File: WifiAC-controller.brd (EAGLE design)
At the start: 55.9 x 53.3 mm, 10 parts

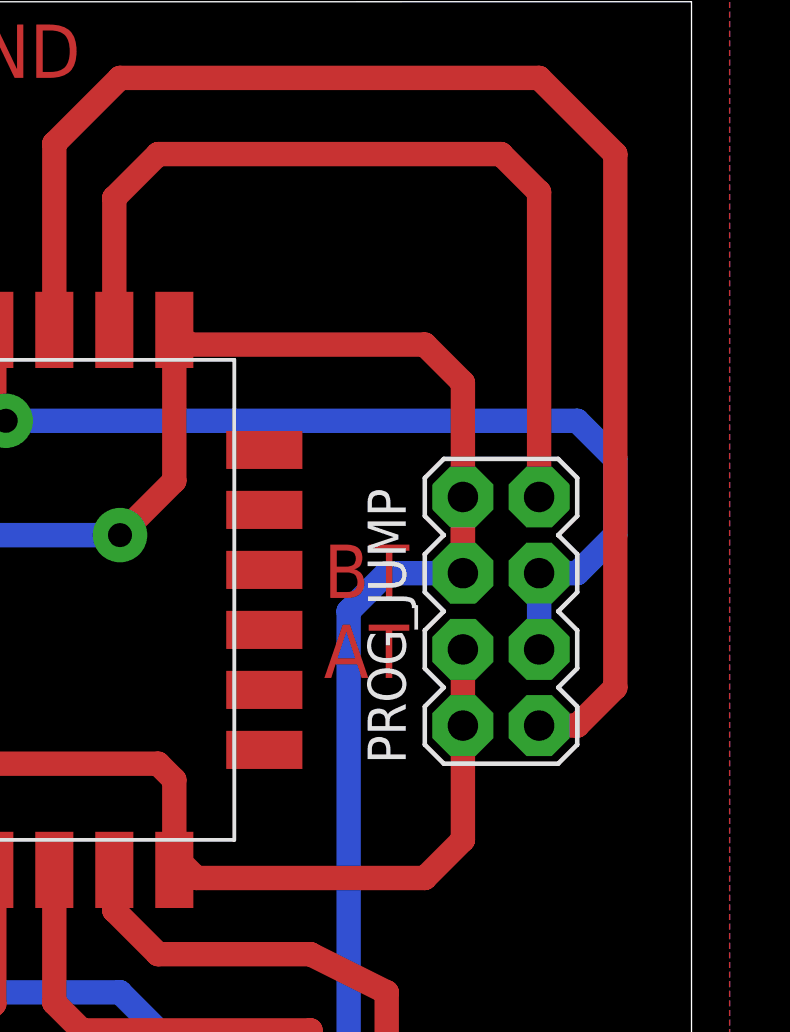
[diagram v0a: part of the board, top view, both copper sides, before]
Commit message: updated schematic to add input connections for the esp module
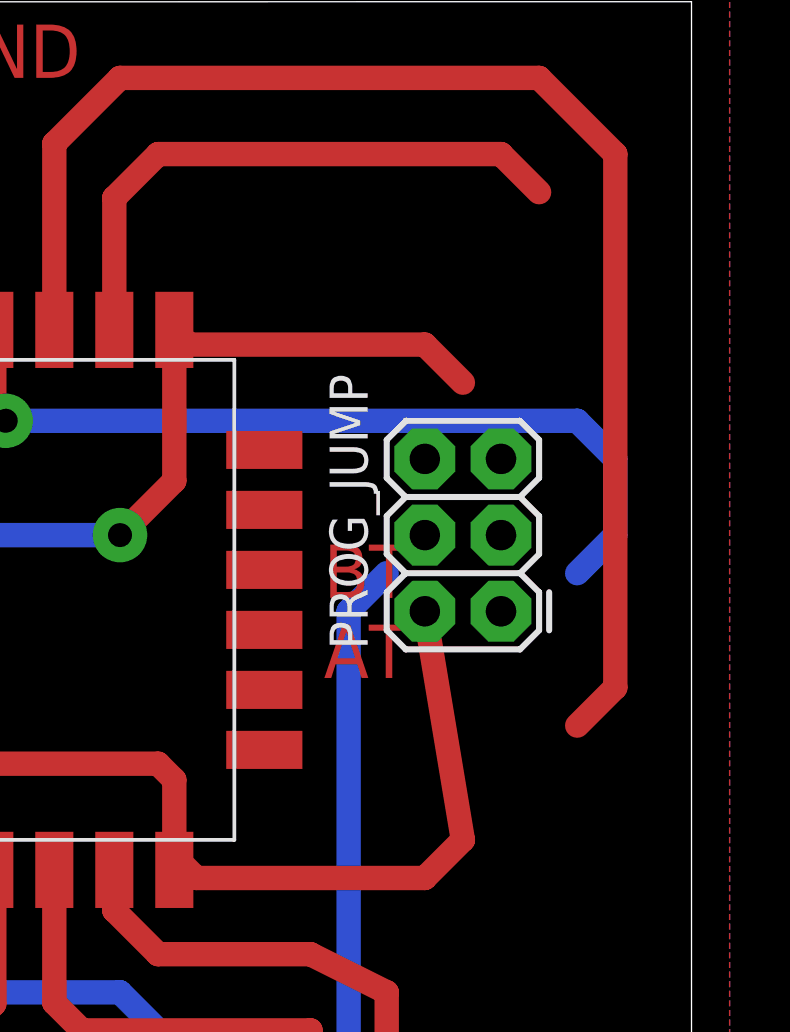
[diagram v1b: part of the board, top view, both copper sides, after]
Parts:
- PROG_JUMP: value (none) -> FEMALE 2x3; device SparkFun-Connectors:2X4 -> SparkFun-Connectors:2X3
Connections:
- net 3V3: no longer PROG_JUMP.4
- net GND: now also PROG_JUMP.4; no longer PROG_JUMP.8
- net GPIO0: no longer PROG_JUMP.5
- net GPIO15: now also PROG_JUMP.5; no longer PROG_JUMP.7
- net P5: now also ESP-12E.GPIO9
- net P58: now also ESP-12E.CSO
- net P59: now also ESP-12E.MISO
- net P6: now also ESP-12E.GPIO10
- net P7: now also ESP-12E.MOSI
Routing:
- net GND: track 123.9 -> 112.5 mm
- net GPIO15: track 29.9 -> 19.7 mm
- net GPIO0: track 32.2 -> 28.4 mm
- net 3V3: track 69.6 -> 71.0 mm
- net GPIO2: track 47.7 -> 46.4 mm
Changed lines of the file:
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@@
 </element>
 <element name="ESP-12E" library="ESP-12E" package="ESP-07/12" value="ESP-07/12_ESP-12E" x="40.64" y="25.4" rot="R90"/>
-<element name="PROG_JUMP" library="SparkFun-Connectors" package="2X4" value="" x="49.53" y="33.02" rot="R90"/>
+<element name="PROG_JUMP" library="SparkFun-Connectors" package="2X3" value="FEMALE 2x3" x="49.53" y="33.02" rot="R90">
+<attribute name="VALUE" value="FEMALE 2x3" x="49.53" y="33.02" size="1.778" layer="27" rot="R90" display="off"/>
+<attribute name="PROD_ID" value="CONN-11566" x="49.53" y="33.02" size="1.778" layer="27" rot="R90" display="off"/>
+</element>
 <element name="PWR_IN" library="SparkFun-Connectors" package="1X02_LOCK_LONGPADS" value="" x="5.08" y="48.26" smashed="yes" rot="R270">
 <attribute name="NAME" x="7.4295" y="51.3715" size="1.27" layer="25" font="vector" rot="R180"/>
@@
 <contactref element="ESP-12E" pad="VCC"/>
 <contactref element="PROG_JUMP" pad="2"/>
-<contactref element="PROG_JUMP" pad="4"/>
 <wire x1="11.56" y1="48.26" x2="11.43" y2="48.26" width="0.8128" layer="1"/>
-<wire x1="48.26" y1="29.21" x2="48.26" y2="31.75" width="0.8128" layer="1"/>
 <wire x1="38.64" y1="24.4" x2="38.64" y2="24.86" width="0.8128" layer="1"/>
 <wire x1="38.64" y1="27.4" x2="38.1" y2="27.94" width="0.8128" layer="1"/>
@@
 <wire x1="39.37" y1="24.13" x2="46.99" y2="24.13" width="0.8128" layer="1"/>
 <wire x1="46.99" y1="24.13" x2="48.26" y2="25.4" width="0.8128" layer="1"/>
-<wire x1="48.26" y1="25.4" x2="48.26" y2="29.21" width="0.8128" layer="1"/>
+<wire x1="48.26" y1="25.4" x2="46.99" y2="33.02" width="0.8128" layer="1"/>
 <wire x1="15.24" y1="49.53" x2="12.83" y2="49.53" width="0.8128" layer="1"/>
 <wire x1="12.83" y1="49.53" x2="11.56" y2="48.26" width="0.8128" layer="1"/>
@@
 <contactref element="RST" pad="3"/>
 <contactref element="TX_RX" pad="1"/>
-<contactref element="PROG_JUMP" pad="6"/>
-<contactref element="PROG_JUMP" pad="8"/>
 <contactref element="QBS_" pad="7"/>
 <wire x1="13.335" y1="37.084" x2="13.335" y2="31.496" width="0.8128" layer="1"/>
-<wire x1="48.26" y1="34.29" x2="48.26" y2="36.83" width="0.8128" layer="1"/>
-<wire x1="48.26" y1="34.29" x2="48.26" y2="40.64" width="0.8128" layer="1"/>
 <wire x1="48.26" y1="40.64" x2="46.99" y2="41.91" width="0.8128" layer="1"/>
 <wire x1="46.99" y1="41.91" x2="39.13" y2="41.91" width="0.8128" layer="1"/>
@@
 <wire x1="44.45" y1="7.62" x2="44.45" y2="33.02" width="0.8128" layer="16"/>
 <wire x1="44.45" y1="33.02" x2="45.72" y2="34.29" width="0.8128" layer="16"/>
-<wire x1="45.72" y1="34.29" x2="48.26" y2="34.29" width="0.8128" layer="16"/>
 <wire x1="13.335" y1="37.084" x2="13.335" y2="37.465" width="0.8128" layer="1"/>
 <wire x1="13.335" y1="37.465" x2="15.24" y2="39.37" width="0.8128" layer="1"/>
@@
 <wire x1="15.24" y1="44.45" x2="15.24" y2="39.37" width="0.8128" layer="16"/>
 <wire x1="27.94" y1="49.53" x2="27.94" y2="35.56" width="0.8128" layer="16"/>
+<contactref element="PROG_JUMP" pad="4"/>
+<contactref element="PROG_JUMP" pad="6"/>
+<wire x1="46.99" y1="35.56" x2="46.99" y2="38.1" width="0" layer="19" extent="1-1"/>
+<wire x1="45.72" y1="34.29" x2="46.99" y2="35.56" width="0" layer="19" extent="16-16"/>
+<wire x1="48.26" y1="40.64" x2="46.99" y2="38.1" width="0" layer="19" extent="1-1"/>
 </signal>
 <signal name="P58">
@@
 <wire x1="31.877" y1="10.033" x2="33.02" y2="8.89" width="0.8128" layer="1"/>
 <wire x1="33.02" y1="8.89" x2="33.02" y2="6.35" width="0.8128" layer="1"/>
+<contactref element="ESP-12E" pad="CSO"/>
+<wire x1="31.877" y1="10.033" x2="41.64" y2="28.4" width="0" layer="19" extent="1-1"/>
 </signal>
 <signal name="P59">
@@
 <wire x1="21.59" y1="10.16" x2="22.86" y2="8.89" width="0.8128" layer="16"/>
 <wire x1="22.86" y1="8.89" x2="25.4" y2="8.89" width="0.8128" layer="16"/>
+<contactref element="ESP-12E" pad="MISO"/>
+<wire x1="38.1" y1="13.97" x2="41.64" y2="30.4" width="0" layer="19" extent="1-1"/>
 </signal>
 <signal name="P5">
@@
 <wire x1="36.83" y1="20.32" x2="40.64" y2="16.51" width="0.8128" layer="16"/>
 <wire x1="40.64" y1="16.51" x2="40.64" y2="13.97" width="0.8128" layer="16"/>
+<contactref element="ESP-12E" pad="GPIO9"/>
+<wire x1="36.83" y1="20.32" x2="41.64" y2="32.4" width="0" layer="19" extent="1-16"/>
 </signal>
 <signal name="P6">
@@
 <wire x1="31.75" y1="17.78" x2="33.02" y2="16.51" width="0.8128" layer="16"/>
 <wire x1="33.02" y1="16.51" x2="33.02" y2="13.97" width="0.8128" layer="16"/>
+<contactref element="ESP-12E" pad="GPIO10"/>
+<wire x1="31.75" y1="17.78" x2="41.64" y2="34.4" width="0" layer="19" extent="1-16"/>
 </signal>
 <signal name="P7">
@@
 <wire x1="3.81" y1="22.86" x2="5.08" y2="24.13" width="0.8128" layer="16"/>
 <wire x1="5.08" y1="24.13" x2="3.81" y2="24.13" width="0.8128" layer="16"/>
+<contactref element="ESP-12E" pad="MOSI"/>
+<wire x1="30.48" y1="6.35" x2="41.64" y2="36.4" width="0" layer="19" extent="1-1"/>
 </signal>
 <signal name="GPIO16">
@@
 <signal name="GPIO0">
 <contactref element="ESP-12E" pad="GPIO0"/>
-<contactref element="PROG_JUMP" pad="3"/>
-<contactref element="PROG_JUMP" pad="5"/>
-<wire x1="50.8" y1="34.29" x2="50.8" y2="31.75" width="0.8128" layer="16"/>
 <wire x1="32.64" y1="42.4" x2="32.64" y2="39.75" width="0.8128" layer="1"/>
 <wire x1="32.64" y1="39.75" x2="33.02" y2="39.37" width="0.8128" layer="1"/>
@@
 <wire x1="53.34" y1="38.1" x2="53.34" y2="35.56" width="0.8128" layer="16"/>
 <wire x1="53.34" y1="35.56" x2="52.07" y2="34.29" width="0.8128" layer="16"/>
-<wire x1="52.07" y1="34.29" x2="50.8" y2="34.29" width="0.8128" layer="16"/>
+<contactref element="PROG_JUMP" pad="3"/>
+<wire x1="52.07" y1="34.29" x2="49.53" y2="35.56" width="0" layer="19" extent="16-16"/>
 </signal>
 <signal name="GPIO2">
 <contactref element="ESP-12E" pad="GPIO2"/>
-<contactref element="PROG_JUMP" pad="1"/>
 <wire x1="34.64" y1="42.4" x2="34.64" y2="48.61" width="0.8128" layer="1"/>
 <wire x1="34.64" y1="48.61" x2="36.83" y2="50.8" width="0.8128" layer="1"/>
@@
 <wire x1="53.34" y1="48.26" x2="53.34" y2="30.48" width="0.8128" layer="1"/>
 <wire x1="53.34" y1="30.48" x2="52.07" y2="29.21" width="0.8128" layer="1"/>
-<wire x1="52.07" y1="29.21" x2="50.8" y2="29.21" width="0.8128" layer="1"/>
+<contactref element="PROG_JUMP" pad="1"/>
+<wire x1="53.34" y1="30.48" x2="49.53" y2="33.02" width="0" layer="19" extent="1-1"/>
 </signal>
 <signal name="GPIO15">
 <contactref element="ESP-12E" pad="GPIO15"/>
-<contactref element="PROG_JUMP" pad="7"/>
 <wire x1="36.64" y1="42.4" x2="36.64" y2="46.8" width="0.8128" layer="1"/>
 <wire x1="36.64" y1="46.8" x2="38.1" y2="48.26" width="0.8128" layer="1"/>
 <wire x1="38.1" y1="48.26" x2="49.53" y2="48.26" width="0.8128" layer="1"/>
 <wire x1="49.53" y1="48.26" x2="50.8" y2="46.99" width="0.8128" layer="1"/>
-<wire x1="50.8" y1="46.99" x2="50.8" y2="36.83" width="0.8128" layer="1"/>
+<contactref element="PROG_JUMP" pad="5"/>
+<wire x1="50.8" y1="46.99" x2="49.53" y2="38.1" width="0" layer="19" extent="1-1"/>
 </signal>
 <signal name="N$2">

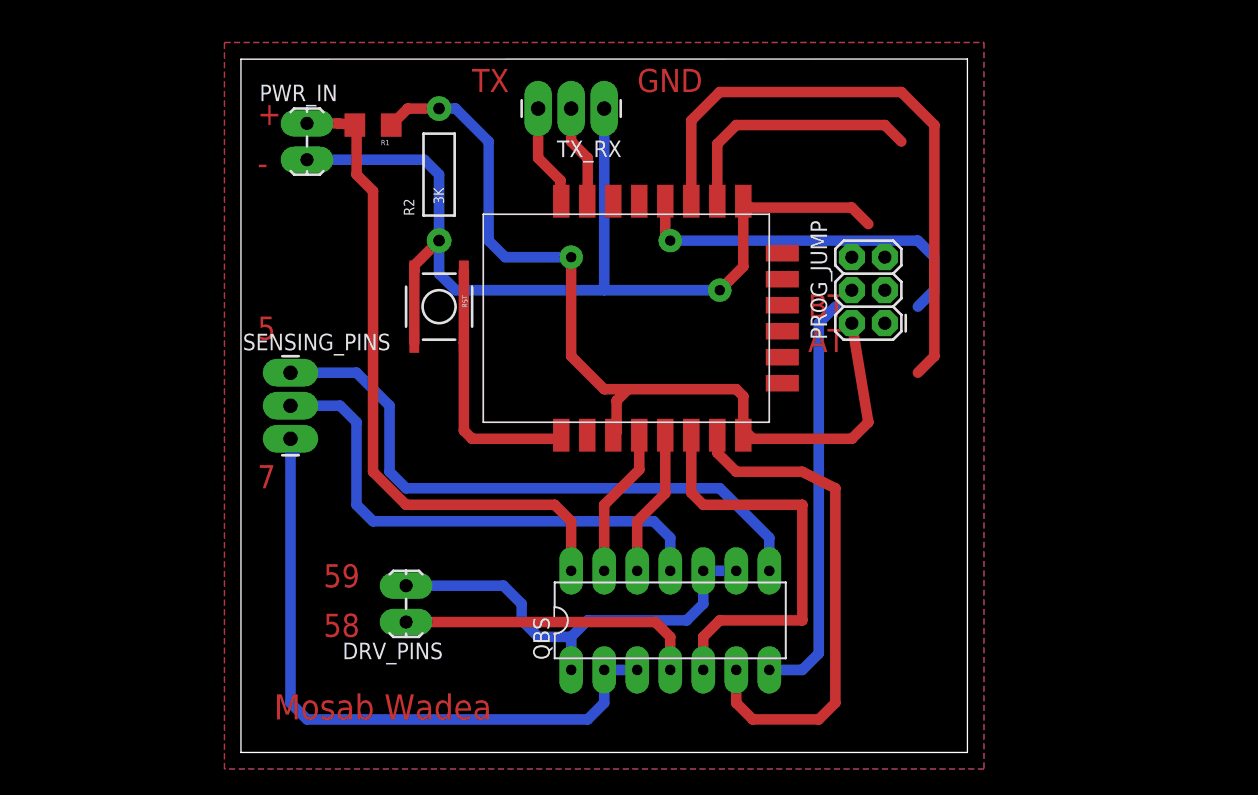
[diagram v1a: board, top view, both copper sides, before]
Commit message: updated layout
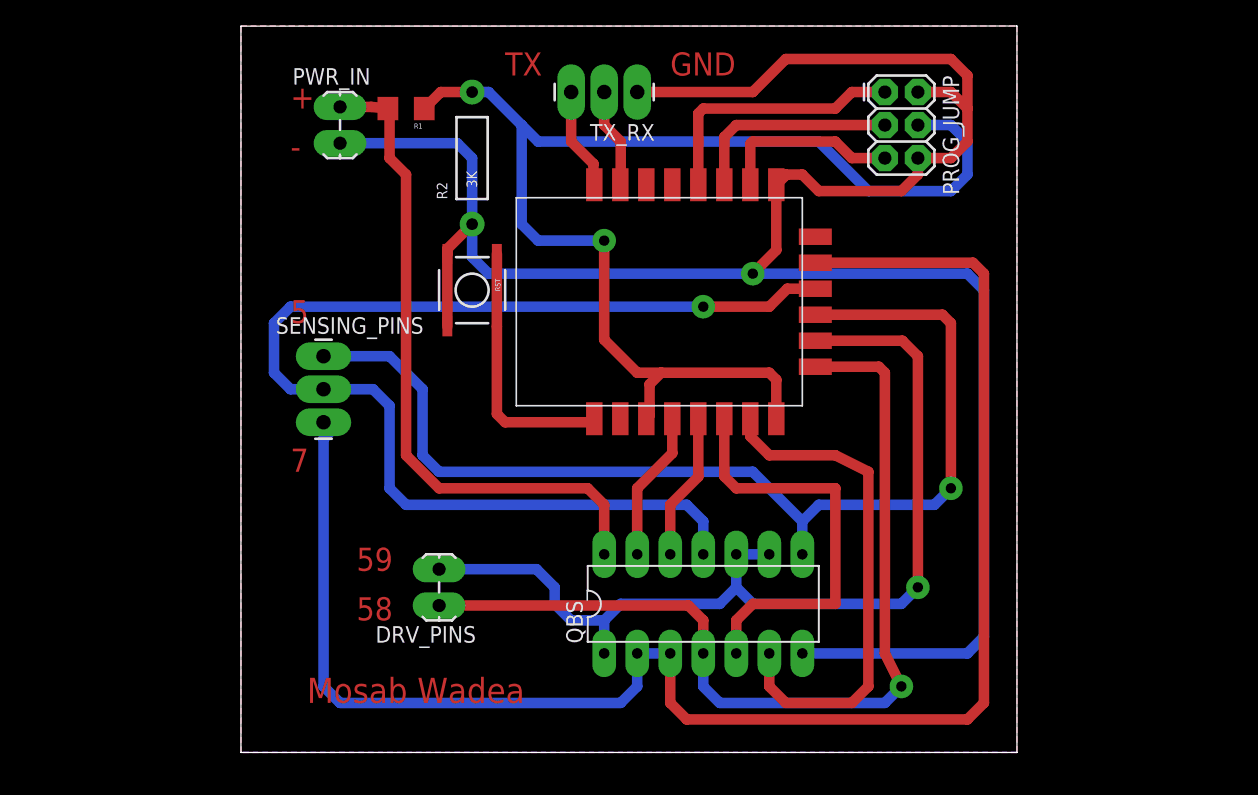
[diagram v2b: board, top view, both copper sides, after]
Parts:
- moved PROG_JUMP 17.8 mm to (49.5, 50.8), turned to 270 degrees
- moved RST 2.84 mm to (17.8, 35.6)
- moved PWR_IN 2.84 mm to (7.62, 49.5)
- moved DRV_PINS 2.84 mm to (15.2, 11.4)
- moved ESP-12E 2.84 mm to (43.2, 26.7)
- moved R1 2.84 mm to (12.7, 49.5)
- moved SENSING_PINS 2.84 mm to (6.35, 30.5)
- moved QBS_ 2.84 mm to (35.6, 11.4)
- moved R2 2.84 mm to (17.8, 45.7)
- moved TX_RX 2.84 mm to (30.5, 50.8)
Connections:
- net 3V3: now also PROG_JUMP.4; no longer PROG_JUMP.2
- net GND: now also PROG_JUMP.2; no longer PROG_JUMP.4
- net GPIO0: now also PROG_JUMP.1; no longer PROG_JUMP.3
- net GPIO2: now also PROG_JUMP.3; no longer PROG_JUMP.1
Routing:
- net P7: track 52.4 -> 127.7 mm
- net GND: track 112.5 -> 170.4 mm
- net P6: track 39.7 -> 90.6 mm, vias 0 -> 1
- net P58: track 23.3 -> 72.1 mm, vias 0 -> 1
- net P59: track 33.9 -> 75.1 mm, vias 0 -> 1
- net P5: track 47.6 -> 83.5 mm, vias 0 -> 1
- net GPIO2: track 46.4 -> 16.4 mm
- net 3V3: track 71.0 -> 96.6 mm
- net GPIO0: track 28.4 -> 20.5 mm, vias 1 -> 0
- net GPIO15: track 19.7 -> 14.1 mm
- added copper zone on layer 1, net GND
- added copper zone on layer 16, net GND
- removed copper zone on layer 16, net N$2
- removed copper zone on layer 1, net N$5
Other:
- board size 55.9 x 53.3 mm -> 59.7 x 55.9 mm
- board text removed: "AT"
- board text removed: "BT"

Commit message: fixes in layout and generated mill path and ref drills
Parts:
- added U$1: (no value), WifiAC-controller~~~ref_tmp:_REFERENCE_HOLE_
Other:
- board size 59.7 x 55.9 mm -> 87.7 x 55.9 mm
